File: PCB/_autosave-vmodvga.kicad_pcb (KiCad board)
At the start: 2 copper layers, 80 x 60.1 mm, 70 parts, among them J1 DE-15, J2 DE-15, J3 VHDCI, P1 50R, P2 50R, P3 50R, P4 50R, P5 CONN_1, P6 CONN_1, U1 ADP3303-3V3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

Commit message: PCB Routing
70% tracks routed. Fine tuning remaining
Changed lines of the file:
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@@
     (links 253)
     (no_connects 2)
-    (area 46.3975 49.249999 167.950001 168.4525)
+    (area 87.849999 49.249999 209.9023 109.450001)
     (thickness 1.6)
     (drawings 7)
@@
   (gr_line (start 167.9 109.35) (end 167.9 49.35) (angle 90) (layer Edge.Cuts) (width 0.1))
   (target plus (at 87.9 109.25) (size 0.005) (width 0.1) (layer Edge.Cuts))
-  (target plus (at 46.4 168.45) (size 0.005) (width 0.1) (layer Edge.Cuts))
+  (target plus (at 209.8998 79.4484) (size 0.005) (width 0.1) (layer Edge.Cuts))
   (segment (start 106.65 87.2) (end 106.65 89.24) (width 0.25) (layer F.Cu) (net 1))
   (segment (start 104.57 91.32) (end 95.05 91.32) (width 0.25) (layer F.Cu) (net 1) (status 20))
@@
   (segment (start 93.01 81.81) (end 92.7 82.12) (width 0.13) (layer B.Cu) (net 18) (status 30))
   (segment (start 94.18 81.81) (end 93.01 81.81) (width 0.13) (layer B.Cu) (net 18) (status 20))
-  (segment (start 94.27 77.11) (end 94.09 76.93) (width 0.13) (layer B.Cu) (net 19))
-  (segment (start 93.09 76.52) (end 91.55 76.52) (width 0.13) (layer B.Cu) (net 19) (status 20))
-  (segment (start 93.5 76.93) (end 93.09 76.52) (width 0.13) (layer B.Cu) (net 19))
-  (segment (start 94.09 76.93) (end 93.5 76.93) (width 0.13) (layer B.Cu) (net 19))
+  (segment (start 94.27 77.11) (end 94.09 76.93) (width 0.125) (layer B.Cu) (net 19))
+  (segment (start 94.09 76.93) (end 93.5 76.93) (width 0.125) (layer B.Cu) (net 19))
+  (segment (start 93.5 76.93) (end 93.09 76.52) (width 0.125) (layer B.Cu) (net 19))
+  (segment (start 93.09 76.52) (end 91.55 76.52) (width 0.125) (layer B.Cu) (net 19) (status 20))
   (segment (start 94.48 77.33) (end 94.48 77.32) (width 0.13) (layer B.Cu) (net 19))
   (segment (start 94.6 77.51) (end 94.6 77.45) (width 0.13) (layer B.Cu) (net 19))

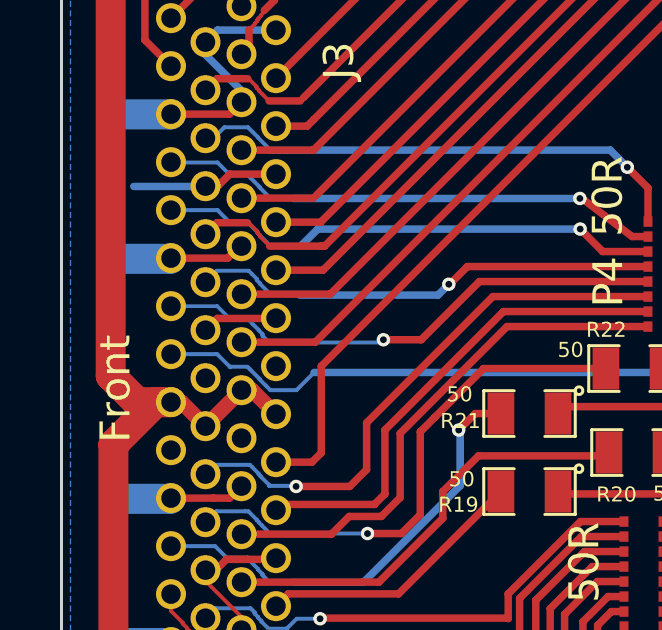
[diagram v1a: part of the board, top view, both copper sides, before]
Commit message: All Tracks routed. Tweaks. Ready for review
All Tracks routed. Tweaks. Ready for review. Some minor changes and
tweaks may be done before sending for Fab
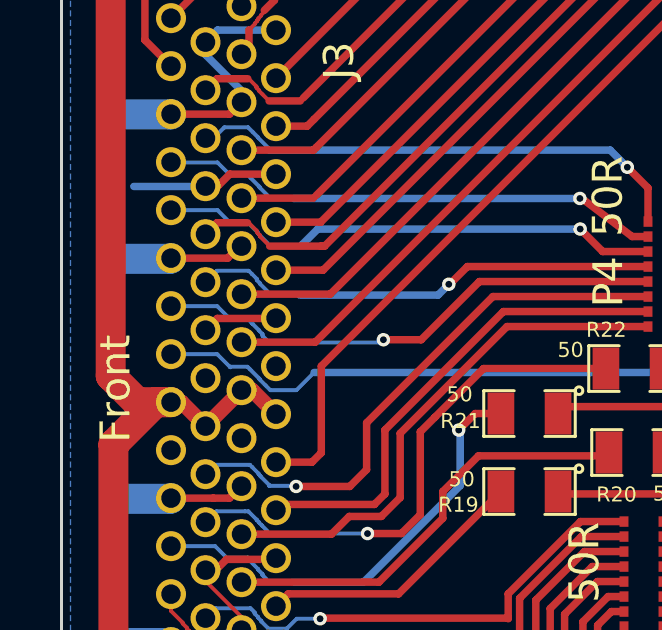
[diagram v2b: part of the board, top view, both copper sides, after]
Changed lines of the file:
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@@
   (segment (start 93.01 81.81) (end 92.7 82.12) (width 0.13) (layer B.Cu) (net 18) (status 30))
   (segment (start 94.18 81.81) (end 93.01 81.81) (width 0.13) (layer B.Cu) (net 18) (status 20))
-  (segment (start 94.27 77.11) (end 94.09 76.93) (width 0.125) (layer B.Cu) (net 19))
-  (segment (start 94.09 76.93) (end 93.5 76.93) (width 0.125) (layer B.Cu) (net 19))
-  (segment (start 93.5 76.93) (end 93.09 76.52) (width 0.125) (layer B.Cu) (net 19))
-  (segment (start 93.09 76.52) (end 91.55 76.52) (width 0.125) (layer B.Cu) (net 19) (status 20))
+  (segment (start 94.27 77.11) (end 94.09 76.93) (width 0.13) (layer B.Cu) (net 19))
+  (segment (start 93.09 76.52) (end 91.55 76.52) (width 0.13) (layer B.Cu) (net 19) (status 20))
+  (segment (start 93.5 76.93) (end 93.09 76.52) (width 0.13) (layer B.Cu) (net 19))
+  (segment (start 94.09 76.93) (end 93.5 76.93) (width 0.13) (layer B.Cu) (net 19))
   (segment (start 94.48 77.33) (end 94.48 77.32) (width 0.13) (layer B.Cu) (net 19))
   (segment (start 94.6 77.51) (end 94.6 77.45) (width 0.13) (layer B.Cu) (net 19))
